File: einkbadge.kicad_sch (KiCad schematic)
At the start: 79 parts, among them J1 USB_C_Receptacle_USB2.0_14P, J2 Conn_01x03, J3 Conn_01x14_Pin, J4 Conn_01x16_Pin, J5 Conn_01x03_Pin, J6 Conn_01x03_Pin, Q1 Si1308EDL, SW1 SW_Push, SW2 SW_Push, SW3 SW_Push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

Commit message: added lcsc part numbers
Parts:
- BOOT1, RESET1: LCSC Part # (none) -> C318884
- C1, C2, C3, C5: LCSC Part # (none) -> C7472957
- C10, C11, C13, C14, C15, C16, C17, C18, C19, C22, C4, C6: LCSC Part # (none) -> C60474
- C12, C9: LCSC Part # (none) -> C5137471
- C20, C21: LCSC Part # (none) -> C7419427
- C23: LCSC Part # (none) -> C5137486
- C24, C25, C26, C27, C28, C29, C30, C31, C32, C33: LCSC Part # (none) -> C5137473
- C7, C8: LCSC Part # (none) -> C325460
- D1, D2, D3: LCSC Part # (none) -> C82046
- D4: LCSC Part # (none) -> C2297
- J1: LCSC Part # (none) -> C2765186
- J5, J6: footprint (none) -> Connector_PinHeader_2.54mm:PinHeader_1x03_P2.54mm_Vertical
- L1: LCSC Part # (none) -> C42411119
- Q1: LCSC Part # (none) -> C7603347
- R1, R2: LCSC Part # (none) -> C2906874
- R10: LCSC Part # (none) -> C93949
- R11, R14, R9: LCSC Part # (none) -> C190095
- R12: LCSC Part # (none) -> C327251
- R13: LCSC Part # (none) -> C854484
- R3: LCSC Part # (none) -> C453643
- R4, R5: LCSC Part # (none) -> C852624
- R6: value 1K -> 1k; LCSC Part # (none) -> C852624
- R7, R8: LCSC Part # (none) -> C2909343
- U1: LCSC Part # (none) -> C151305
- U2: LCSC Part # (none) -> C41378174
- U3: LCSC Part # (none) -> C20546
- U4: LCSC Part # (none) -> C2654815
- U5: LCSC Part # C262567 -> C262643
- Y1: LCSC Part # (none) -> C20625731
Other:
- note removed: "- add on led"
- note removed: "CHECK THIS FOOTPRINT"
- note removed: "led turns on when nfc is used?"

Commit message: update
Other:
- note removed: "LOOK AT DESIGN GUIDE FOR PCB LAYOUT FOR VREG"
- note removed: "place resistors close to mcu"
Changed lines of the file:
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@@
-		)
-	)
-	(text "place resistors close to mcu"
-		(exclude_from_sim no)
-		(at 220.726 170.942 0)
-		(effects
-			(font
-				(size 1.27 1.27)
-			)
 		)
 	)
@@
 			)
 		)
-	)
-	(text "LOOK AT DESIGN GUIDE FOR PCB LAYOUT FOR VREG"
-		(exclude_from_sim no)
-		(at 43.942 173.228 0)
-		(effects
-			(font
-				(size 1.27 1.27)
-			)
-		)

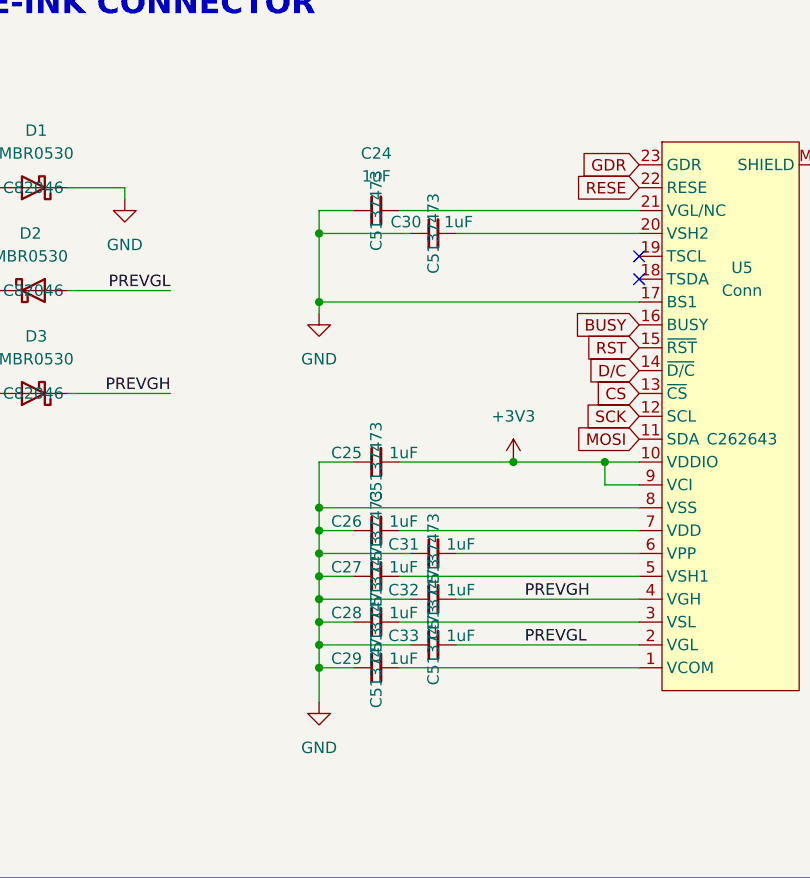
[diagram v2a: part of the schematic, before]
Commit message: update 1uf lcsc part
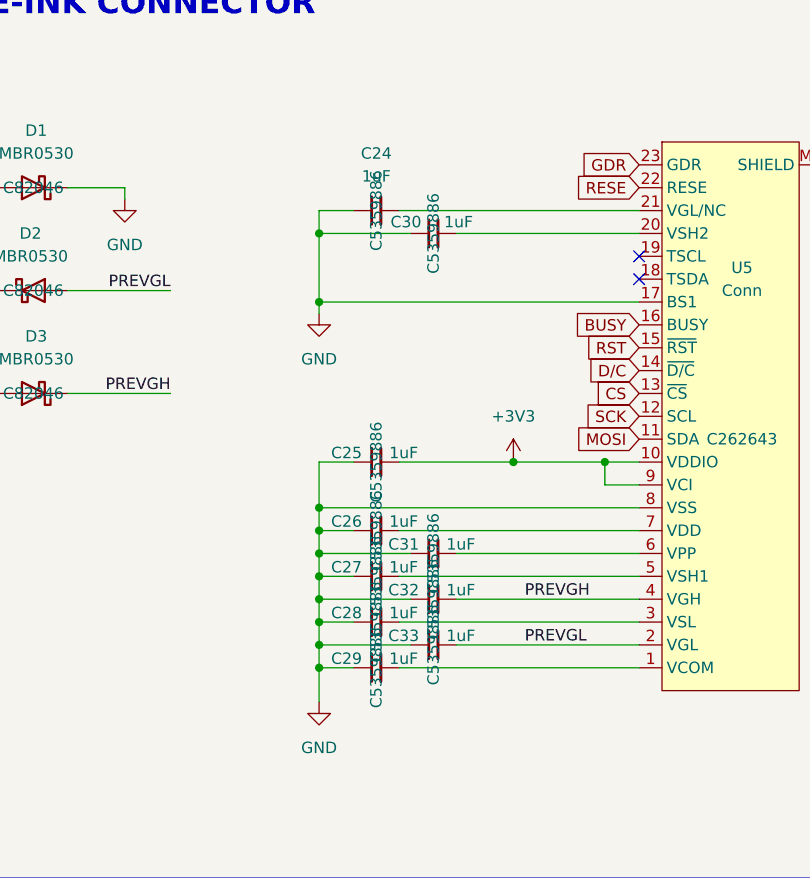
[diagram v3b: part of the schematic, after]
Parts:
- C24, C25, C26, C27, C28, C29, C30, C31, C32, C33: LCSC Part # C5137473 -> C5359886
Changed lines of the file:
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@@
 			)
 		)
-		(property "LCSC Part #" "C5137473"
+		(property "LCSC Part #" "C5359886"
 			(at 407.67 97.79 0)
 			(effects
@@
 			)
 		)
-		(property "LCSC Part #" "C5137473"
+		(property "LCSC Part #" "C5359886"
 			(at 407.67 92.71 0)
 			(effects
@@
 			)
 		)
-		(property "LCSC Part #" "C5137473"
+		(property "LCSC Part #" "C5359886"
 			(at 401.32 54.61 0)
 			(effects
@@
 			)
 		)
-		(property "LCSC Part #" "C5137473"
+		(property "LCSC Part #" "C5359886"
 			(at 407.67 102.87 0)
 			(effects
@@
 			)
 		)
-		(property "LCSC Part #" "C5137473"
+		(property "LCSC Part #" "C5359886"
 			(at 401.32 105.41 0)
 			(effects
@@
 			)
 		)
-		(property "LCSC Part #" "C5137473"
+		(property "LCSC Part #" "C5359886"
 			(at 401.32 90.17 0)
 			(effects
@@
 			)
 		)
-		(property "LCSC Part #" "C5137473"
+		(property "LCSC Part #" "C5359886"
 			(at 407.67 57.15 0)
 			(effects
@@
 			)
 		)
-		(property "LCSC Part #" "C5137473"
+		(property "LCSC Part #" "C5359886"
 			(at 401.32 82.55 0)
 			(effects
@@
 			)
 		)
-		(property "LCSC Part #" "C5137473"
+		(property "LCSC Part #" "C5359886"
 			(at 401.32 95.25 0)
 			(effects
@@
 			)
 		)
-		(property "LCSC Part #" "C5137473"
+		(property "LCSC Part #" "C5359886"
 			(at 401.32 100.33 0)
 			(effects

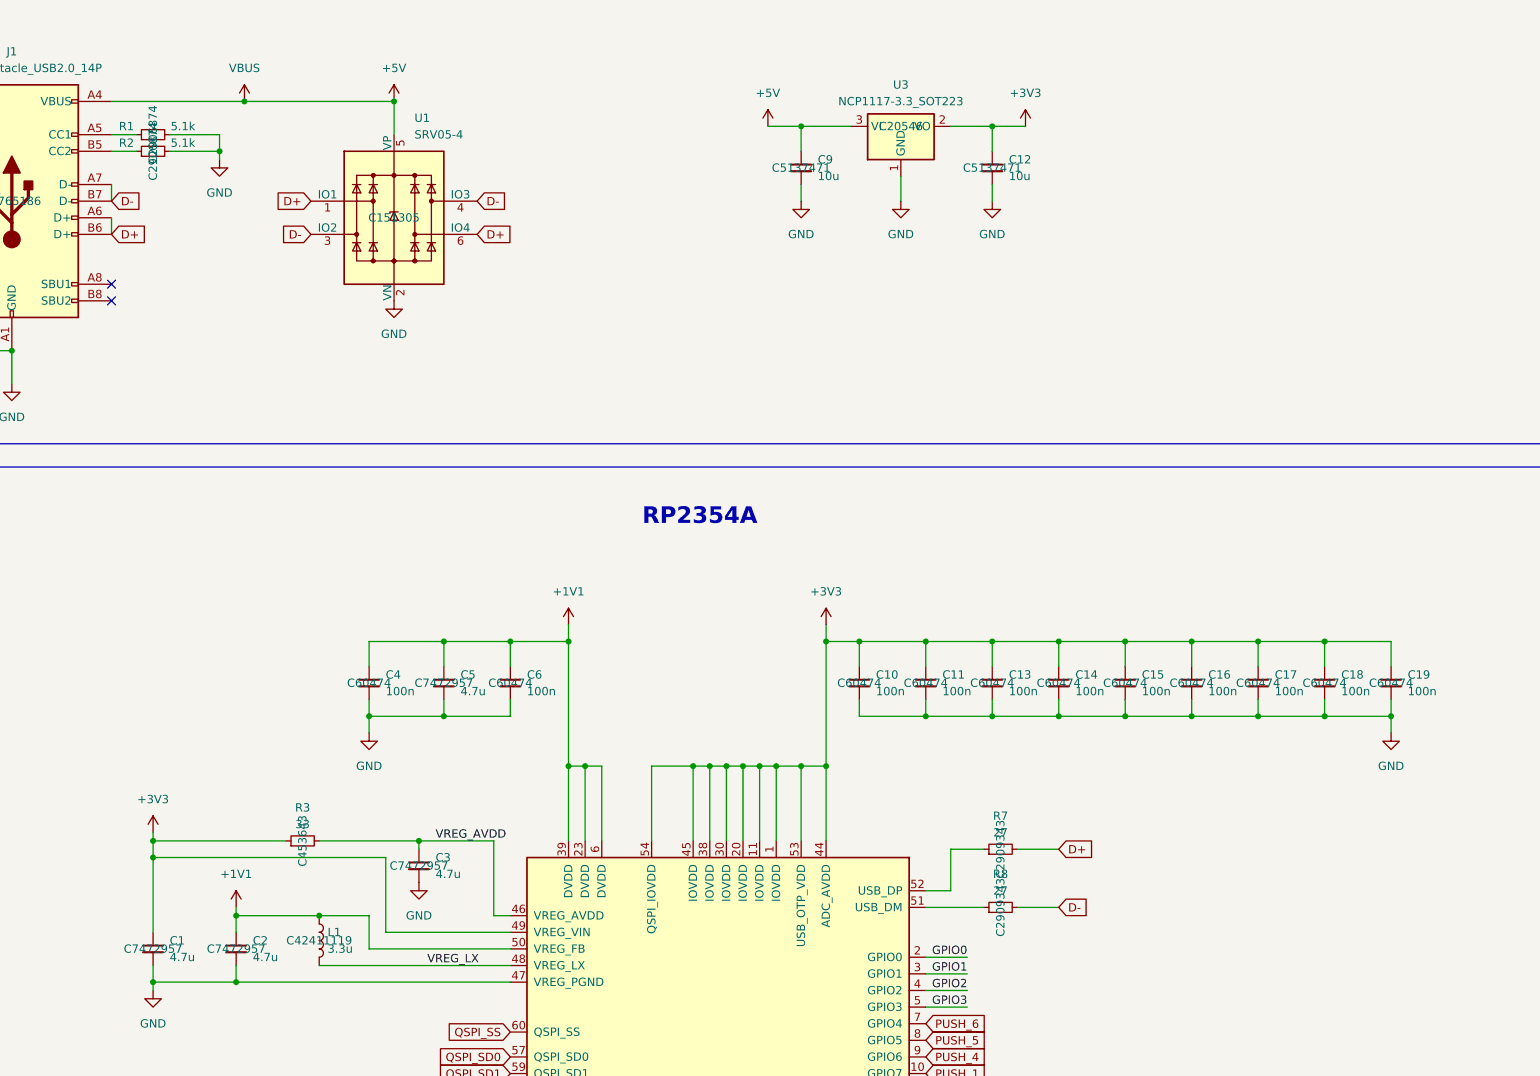
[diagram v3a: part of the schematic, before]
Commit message: Update silkscreen, soldermask and MPNs
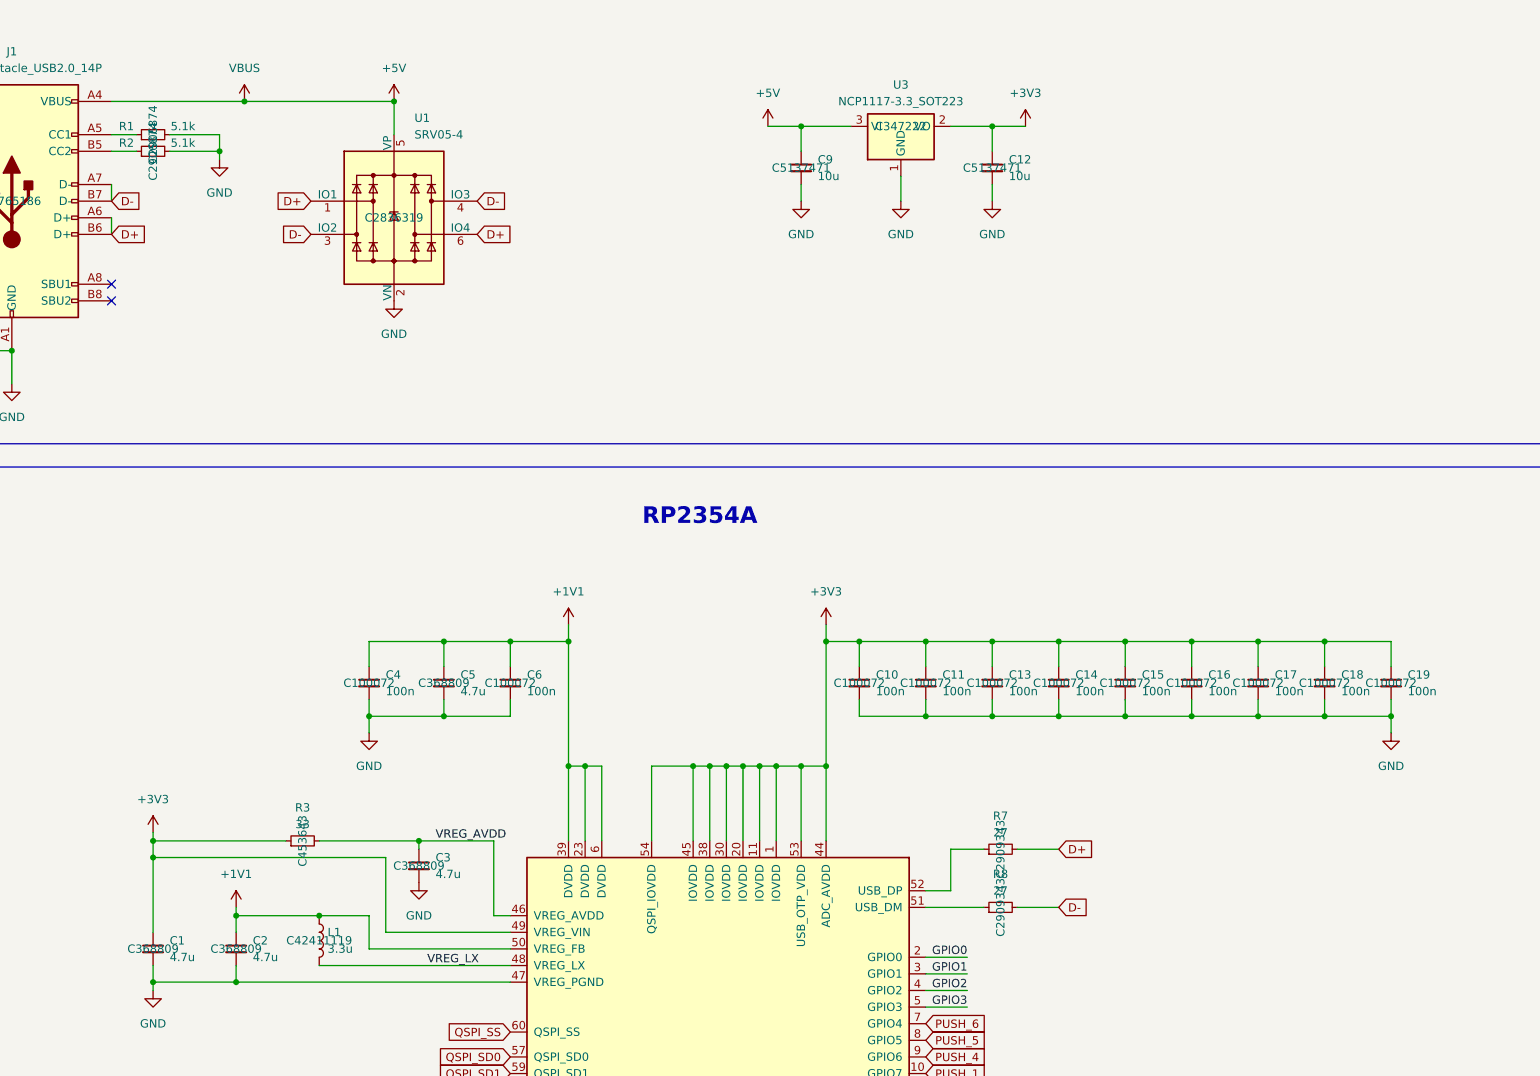
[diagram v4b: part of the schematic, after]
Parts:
- C1, C2, C3, C5: LCSC Part # C7472957 -> C368809
- C10, C11, C13, C14, C15, C16, C17, C18, C19, C4, C6: LCSC Part # C60474 -> C100072
- U1: LCSC Part # C151305 -> C2836319
- U3: LCSC Part # C20546 -> C347222
